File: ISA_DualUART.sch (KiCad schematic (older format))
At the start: 2 parts, among them J1 ISA BUS, X1 1.8432Mhz

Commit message: Begin adding components
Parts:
- added U? (x2): GD75232N, Package_DIP:DIP-20_W7.62mm_LongPads, symbol Interface_UART:GD75232N
- added U? (x2): 16550, Package_DIP:DIP-40_W15.24mm_LongPads, symbol Interface_UART:16550
- added U? (x2): 74LS138, Package_DIP:DIP-16_W7.62mm_LongPads, symbol 74xx:74LS138
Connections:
- net VCC: now reaches X1.14 (Vcc)
- net GND: now reaches X1.7 (GND)
- net SER_CLK: now reaches X1.8 (OUT)
- no-connect marks 0 -> 1
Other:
- moved on the sheet: J1, X1
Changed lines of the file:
@@
 EELAYER 30 0
 EELAYER END
-$Descr A4 11693 8268
+$Descr A3 16535 11693
 encoding utf-8
 Sheet 1 1
 Title ""
 Date ""
-Rev ""
+Rev "1.0"
 Comp ""
 Comment1 ""
@@
 L Connector:Bus_ISA_8bit J1
 U 1 1 60040338
-P 2250 3050
-F 0 "J1" H 2250 4817 50  0000 C CNN
-F 1 "ISA BUS" H 2250 4726 50  0000 C CNN
-F 2 "skiselev_footprints:Conn_Edge_PCB_ISA8" H 2250 3050 50  0001 C CNN
-F 3 "https://en.wikipedia.org/wiki/Industry_Standard_Architecture" H 2250 3050 50  0001 C CNN
-	1    2250 3050
+P 2100 5700
+F 0 "J1" H 2100 7467 50  0000 C CNN
+F 1 "ISA BUS" H 2100 7376 50  0000 C CNN
+F 2 "skiselev_footprints:Conn_Edge_PCB_ISA8" H 2100 5700 50  0001 C CNN
+F 3 "https://en.wikipedia.org/wiki/Industry_Standard_Architecture" H 2100 5700 50  0001 C CNN
+	1    2100 5700
 	1    0    0    -1
 $EndComp
@@
 L Oscillator:CXO_DIP14 X1
 U 1 1 60044D3C
-P 5450 1450
-F 0 "X1" H 5250 1700 50  0000 L CNN
-F 1 "1.8432Mhz" H 5500 1700 50  0000 L CNN
-F 2 "ISA_DualUART:Oscillator_DIP-14-8" H 5900 1100 50  0001 C CNN
-F 3 "http://cdn-reichelt.de/documents/datenblatt/B400/OSZI.pdf" H 5350 1450 50  0001 C CNN
-	1    5450 1450
+P 1400 1350
+F 0 "X1" H 1200 1600 50  0000 L CNN
+F 1 "1.8432Mhz" H 1450 1600 50  0000 L CNN
+F 2 "ISA_DualUART:Oscillator_DIP-14-8" H 1850 1000 50  0001 C CNN
+F 3 "http://cdn-reichelt.de/documents/datenblatt/B400/OSZI.pdf" H 1300 1350 50  0001 C CNN
+	1    1400 1350
 	1    0    0    -1
 $EndComp
+$Comp
+L power:VCC #PWR?
+U 1 1 60049140
+P 1400 950
+F 0 "#PWR?" H 1400 800 50  0001 C CNN
+F 1 "VCC" H 1415 1123 50  0000 C CNN
+F 2 "" H 1400 950 50  0001 C CNN
+F 3 "" H 1400 950 50  0001 C CNN
+	1    1400 950
+	1    0    0    -1
+$EndComp
+Wire Wire Line
+	1400 950  1400 1050
+$Comp
+L power:GND #PWR?
+U 1 1 60049961
+P 1400 1750
+F 0 "#PWR?" H 1400 1500 50  0001 C CNN
+F 1 "GND" H 1405 1577 50  0000 C CNN
+F 2 "" H 1400 1750 50  0001 C CNN
+F 3 "" H 1400 1750 50  0001 C CNN
+	1    1400 1750
+	1    0    0    -1
+$EndComp
+Wire Wire Line
+	1400 1650 1400 1750
+Wire Wire Line
+	1100 1350 900  1350
+NoConn ~ 900  1350
+Wire Wire Line
+	1700 1350 2300 1350
+Text Label 2300 1350 2    50   ~ 0
+SER_CLK
+$Comp
+L Interface_UART:GD75232N U?
+U 1 1 60051101
+P 11900 6400
+F 0 "U?" H 11500 7000 50  0000 C CNN
+F 1 "GD75232N" H 12300 7000 50  0000 C CNN
+F 2 "Package_DIP:DIP-20_W7.62mm_LongPads" H 11900 5600 50  0001 C CIN
+F 3 "http://www.ti.com/lit/ds/symlink/gd75232.pdf" H 11400 6400 50  0001 C CNN
+	1    11900 6400
+	1    0    0    -1
+$EndComp
+$Comp
+L Interface_UART:GD75232N U?
+U 1 1 60051F94
+P 13650 6400
+F 0 "U?" H 13250 7000 50  0000 C CNN
+F 1 "GD75232N" H 14050 7000 50  0000 C CNN
+F 2 "Package_DIP:DIP-20_W7.62mm_LongPads" H 13650 5600 50  0001 C CIN
+F 3 "http://www.ti.com/lit/ds/symlink/gd75232.pdf" H 13150 6400 50  0001 C CNN
+	1    13650 6400
+	1    0    0    -1
+$EndComp
+$Comp
+L Interface_UART:16550 U?
+U 1 1 60054173
+P 5200 3200
+F 0 "U?" H 5200 5081 50  0000 C CNN
+F 1 "16550" H 5200 4990 50  0000 C CNN
+F 2 "Package_DIP:DIP-40_W15.24mm_LongPads" H 5200 3200 50  0001 C CIN
+F 3 "http://www.ti.com/lit/ds/symlink/pc16550d.pdf" H 5200 3200 50  0001 C CNN
+	1    5200 3200
+	1    0    0    -1
+$EndComp
+$Comp
+L Interface_UART:16550 U?
+U 1 1 6005ACD0
+P 8250 3200
+F 0 "U?" H 8250 5081 50  0000 C CNN
+F 1 "16550" H 8250 4990 50  0000 C CNN
+F 2 "Package_DIP:DIP-40_W15.24mm_LongPads" H 8250 3200 50  0001 C CIN
+F 3 "http://www.ti.com/lit/ds/symlink/pc16550d.pdf" H 8250 3200 50  0001 C CNN
+	1    8250 3200
+	1    0    0    -1
+$EndComp
+$Comp
+L 74xx:74LS138 U?
+U 1 1 6005EE46
+P 11600 3750
+F 0 "U?" H 11600 4531 50  0000 C CNN
+F 1 "74LS138" H 11600 4440 50  0000 C CNN
+F 2 "Package_DIP:DIP-16_W7.62mm_LongPads" H 11600 3750 50  0001 C CNN
+F 3 "http://www.ti.com/lit/gpn/sn74LS138" H 11600 3750 50  0001 C CNN
+	1    11600 3750
+	1    0    0    -1
+$EndComp
+$Comp
+L 74xx:74LS138 U?
+U 1 1 6005F673
+P 12950 3750
+F 0 "U?" H 12950 4531 50  0000 C CNN
+F 1 "74LS138" H 12950 4440 50  0000 C CNN
+F 2 "Package_DIP:DIP-16_W7.62mm_LongPads" H 12950 3750 50  0001 C CNN
+F 3 "http://www.ti.com/lit/gpn/sn74LS138" H 12950 3750 50  0001 C CNN
+	1    12950 3750
+	1    0    0    -1
+$EndComp

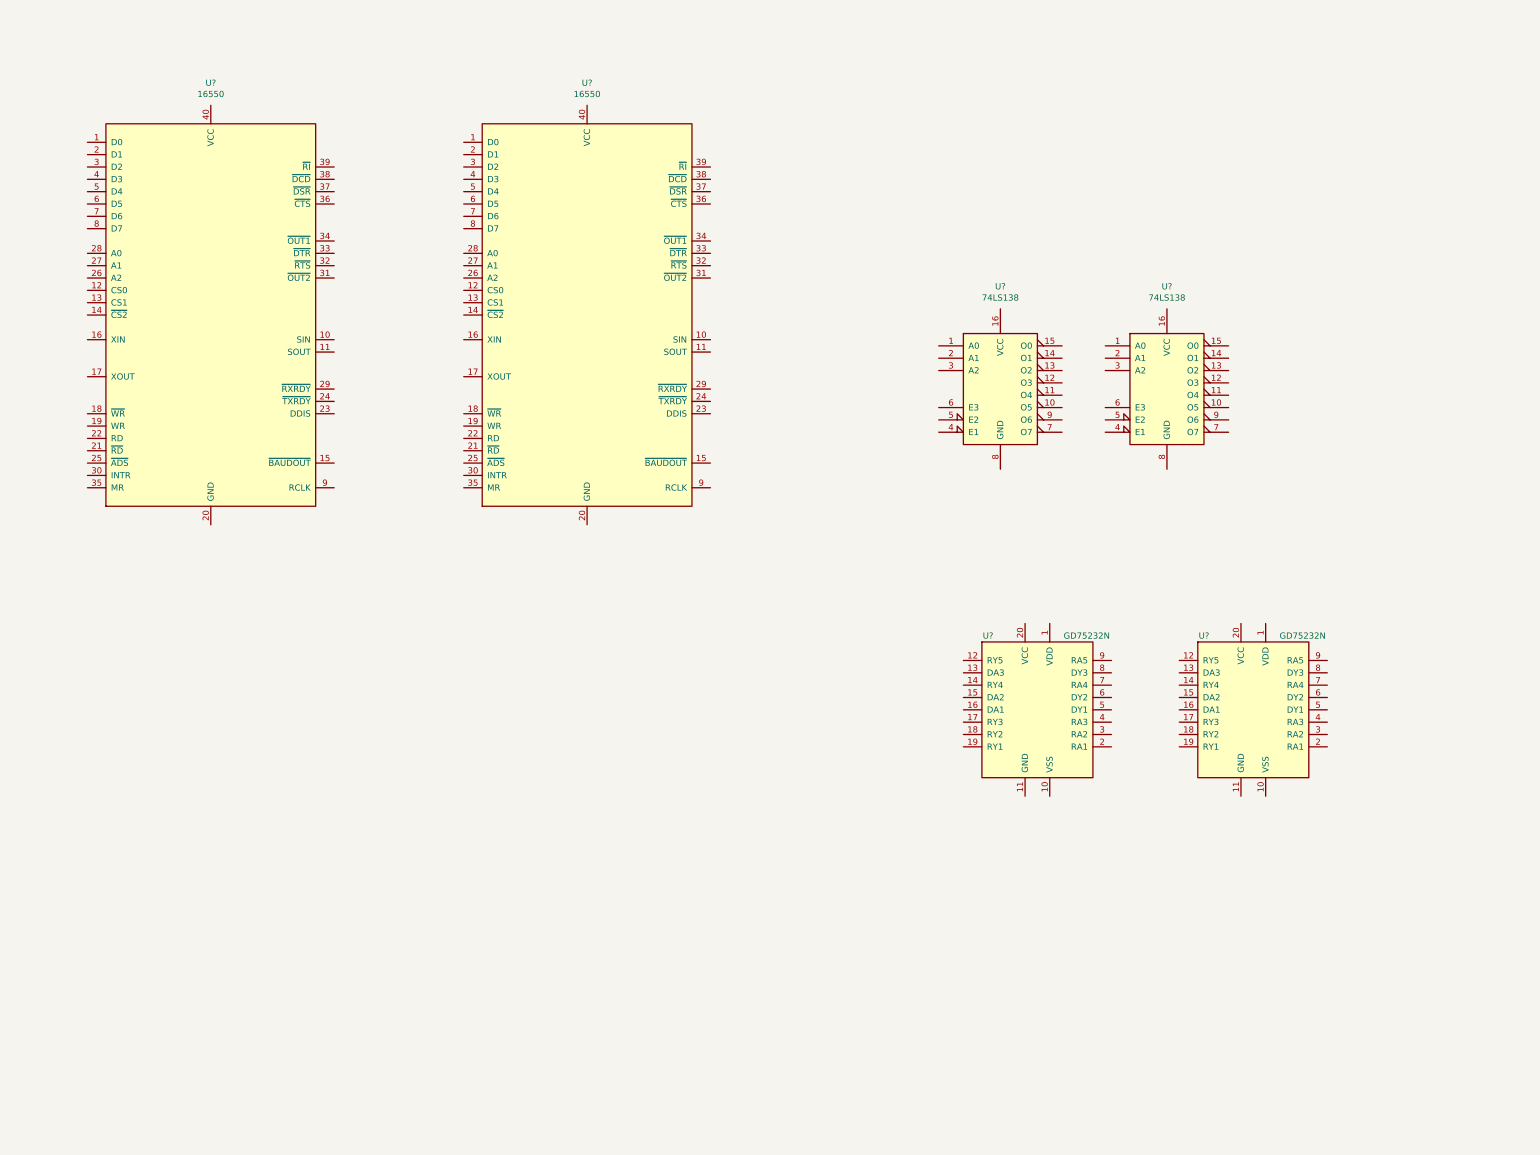
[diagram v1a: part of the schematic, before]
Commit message: Added all the required ICs
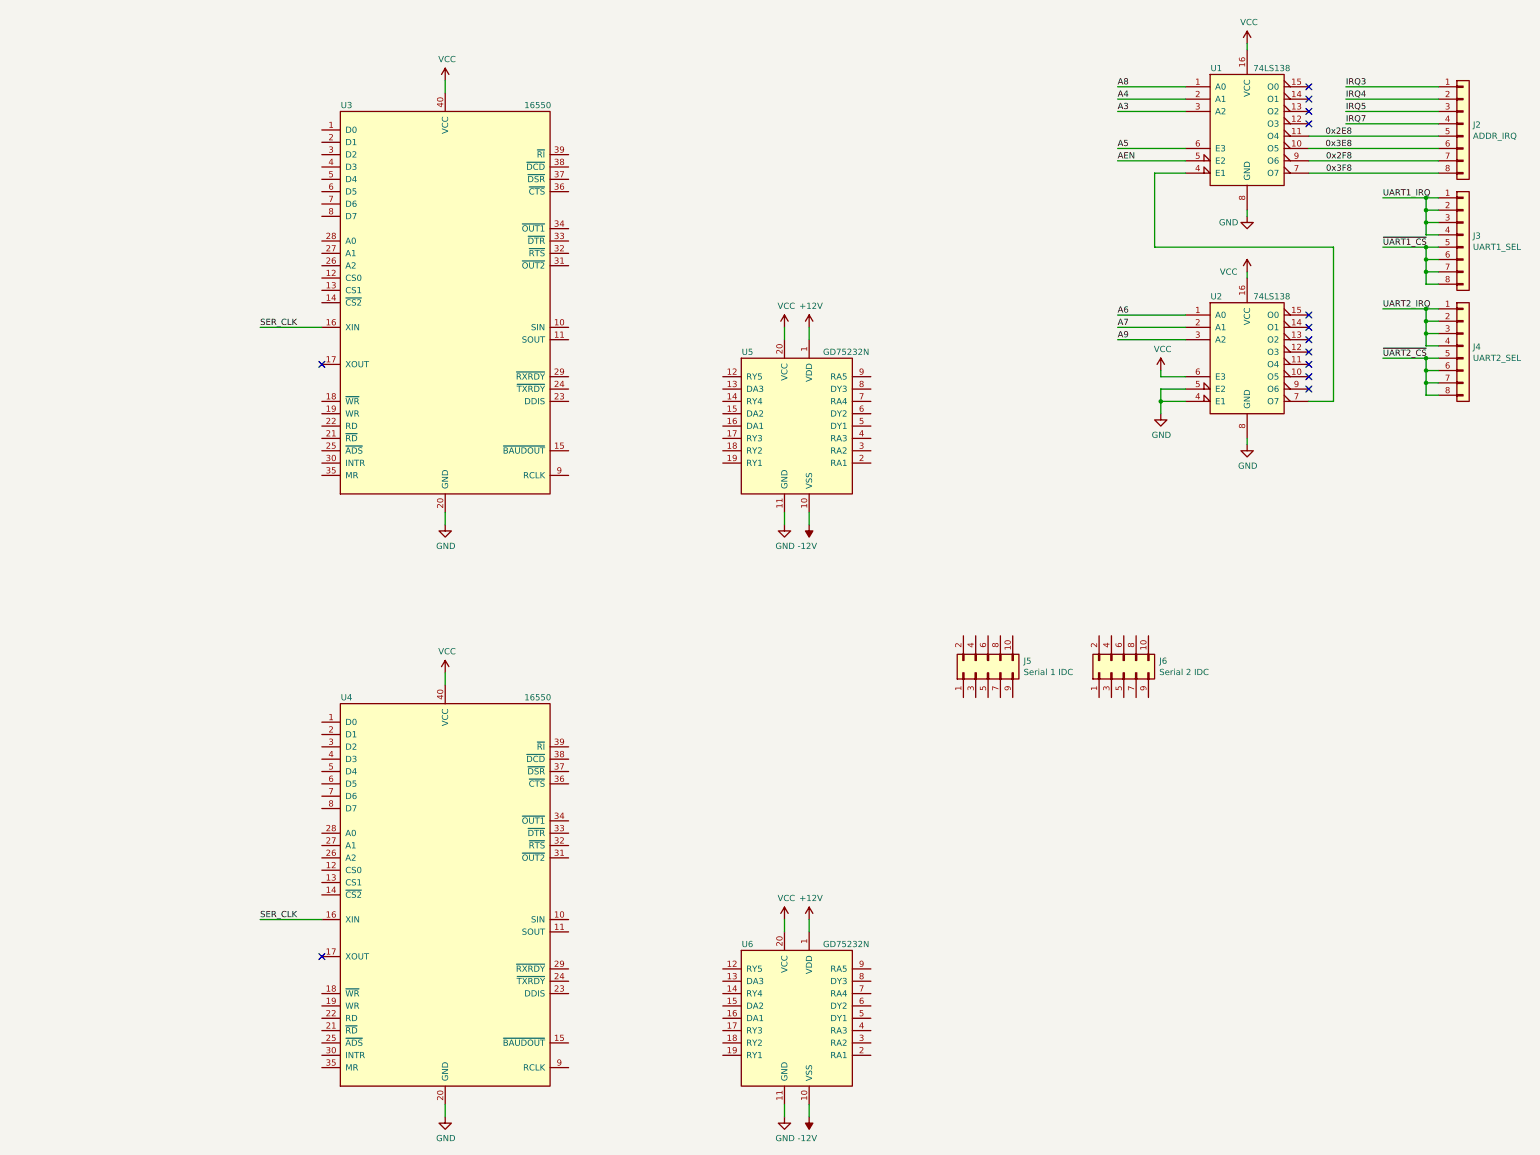
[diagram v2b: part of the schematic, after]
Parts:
- removed U?: GD75232N, Package_DIP:DIP-20_W7.62mm_LongPads, symbol Interface_UART:GD75232N
- removed U?: 16550, Package_DIP:DIP-40_W15.24mm_LongPads, symbol Interface_UART:16550
- added J2: ADDR_IRQ, Connector_PinHeader_2.54mm:PinHeader_1x08_P2.54mm_Vertical, symbol Connector_Generic:Conn_01x08
- added J3: UART1_SEL, Connector_PinHeader_2.54mm:PinHeader_1x08_P2.54mm_Vertical, symbol Connector_Generic:Conn_01x08
- added J4: UART2_SEL, Connector_PinHeader_2.54mm:PinHeader_1x08_P2.54mm_Vertical, symbol Connector_Generic:Conn_01x08
- added J5: Serial 1 IDC, Connector_PinHeader_2.54mm:PinHeader_2x04_P2.54mm_Vertical, symbol Connector_Generic:Conn_02x05_Odd_Even
- added J6: Serial 2 IDC, Connector_PinHeader_2.54mm:PinHeader_2x04_P2.54mm_Vertical, symbol Connector_Generic:Conn_02x05_Odd_Even
- added U4: 16550, Package_DIP:DIP-40_W15.24mm_LongPads, symbol Interface_UART:16550
- added U6: GD75232N, Package_DIP:DIP-20_W7.62mm_LongPads, symbol Interface_UART:GD75232N
- gave numbers to parts that had none: 4
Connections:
- net GND: now also U1.8 (GND), U2.4 (E1), U2.5 (E2), U2.8 (GND), U3.20 (GND), U5.11 (GND), U4.20 (GND), U6.11 (GND)
- net SER_CLK: now also U3.16 (XIN), U4.16 (XIN)
- net VCC: now also U1.16 (VCC), U2.16 (VCC), U2.6 (E3), U3.40 (VCC), U5.20 (VCC), U4.40 (VCC), U6.20 (VCC)
- net +12V: now reaches U5.1 (VDD)
- net +12V: now also U6.1 (VDD)
- net -12V: now reaches U5.10 (VSS)
- net -12V: now also U6.10 (VSS)
- net A6: now reaches U2.1 (A0)
- net A7: now reaches U2.2 (A1)
- net A9: now reaches U2.3 (A2)
- net at U2.7 (O7): now also U1.4 (E1)
- net A8: now reaches U1.1 (A0)
- net 0x3E8: now reaches U1.10 (O5)
- net 0x3E8: now also J2.6 (Pin_6)
- net 0x2E8: now reaches U1.11 (O4)
- net 0x2E8: now also J2.5 (Pin_5)
- net A4: now reaches U1.2 (A1)
- net A3: now reaches U1.3 (A2)
- net AEN: now reaches U1.5 (E2)
- net A5: now reaches U1.6 (E3)
- net 0x3F8: now reaches U1.7 (O7)
- net 0x3F8: now also J2.8 (Pin_8)
- net 0x2F8: now reaches U1.9 (O6)
- net 0x2F8: now also J2.7 (Pin_7)
- new net IRQ3: J2.1 (Pin_1)
- new net IRQ4: J2.2 (Pin_2)
- new net IRQ5: J2.3 (Pin_3)
- new net IRQ7: J2.4 (Pin_4)
- new net UART1_IRQ: J3.1 (Pin_1), J3.2 (Pin_2), J3.3 (Pin_3), J3.4 (Pin_4)
- new net UART2_IRQ: J4.1 (Pin_1), J4.2 (Pin_2), J4.3 (Pin_3), J4.4 (Pin_4)
- new net ~UART1_CS: J3.5 (Pin_5), J3.6 (Pin_6), J3.7 (Pin_7), J3.8 (Pin_8)
- new net ~UART2_CS: J4.5 (Pin_5), J4.6 (Pin_6), J4.7 (Pin_7), J4.8 (Pin_8)
- no-connect marks 1 -> 14
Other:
- moved on the sheet: U1, U2, U3, U5
